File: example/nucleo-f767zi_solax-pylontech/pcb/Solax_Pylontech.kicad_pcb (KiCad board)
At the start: 2 copper layers, 34 x 86 mm, 37 parts, among them J1 Conn_02x10_Odd_Even, J2 Conn_02x07_Odd_Even, U1 LT1107CS, U2 MCP2551-I-SN, U3 MCP2551-I-SN

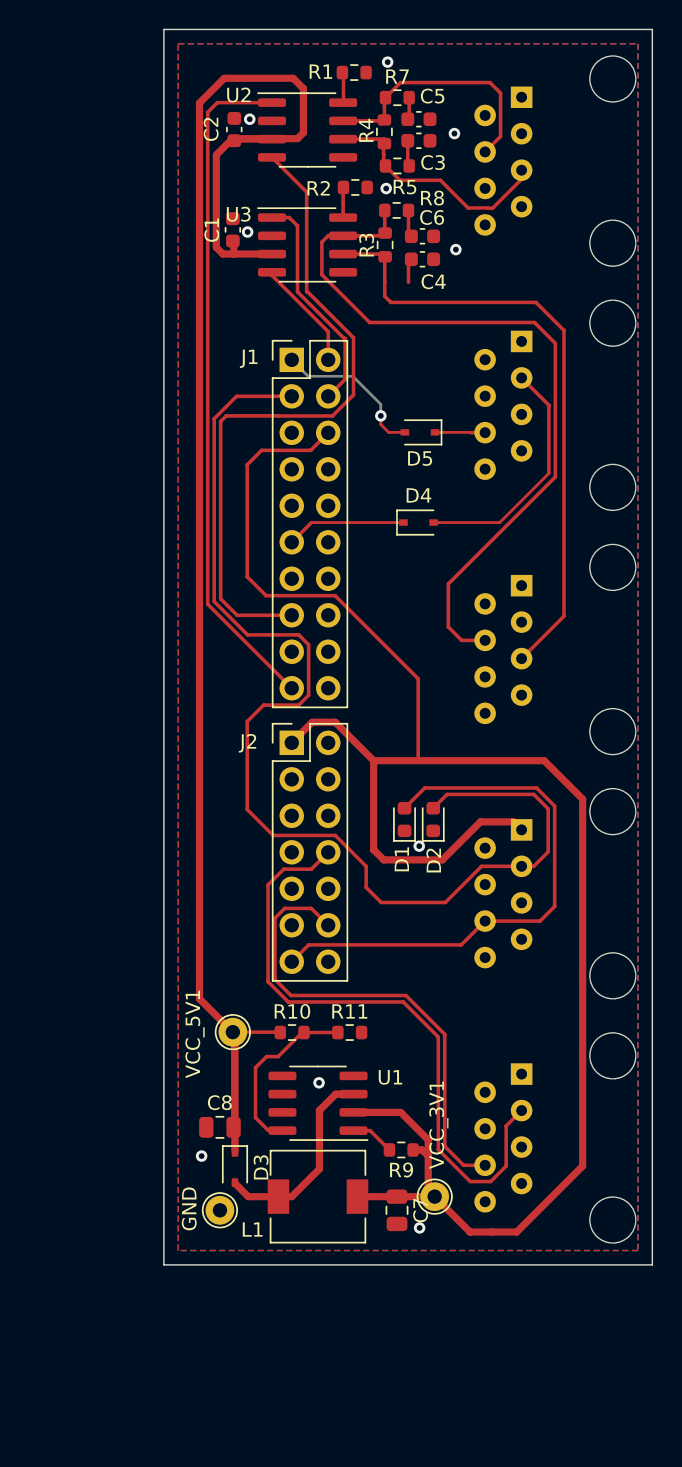
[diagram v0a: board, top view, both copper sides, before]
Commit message: - implement battery balancing using external charger in front of each pack (HDR-15-48), each one driven by a triac module (MRA-23D2) - add home assistant shenanigans to drive the battery balancing (manual or automatic)
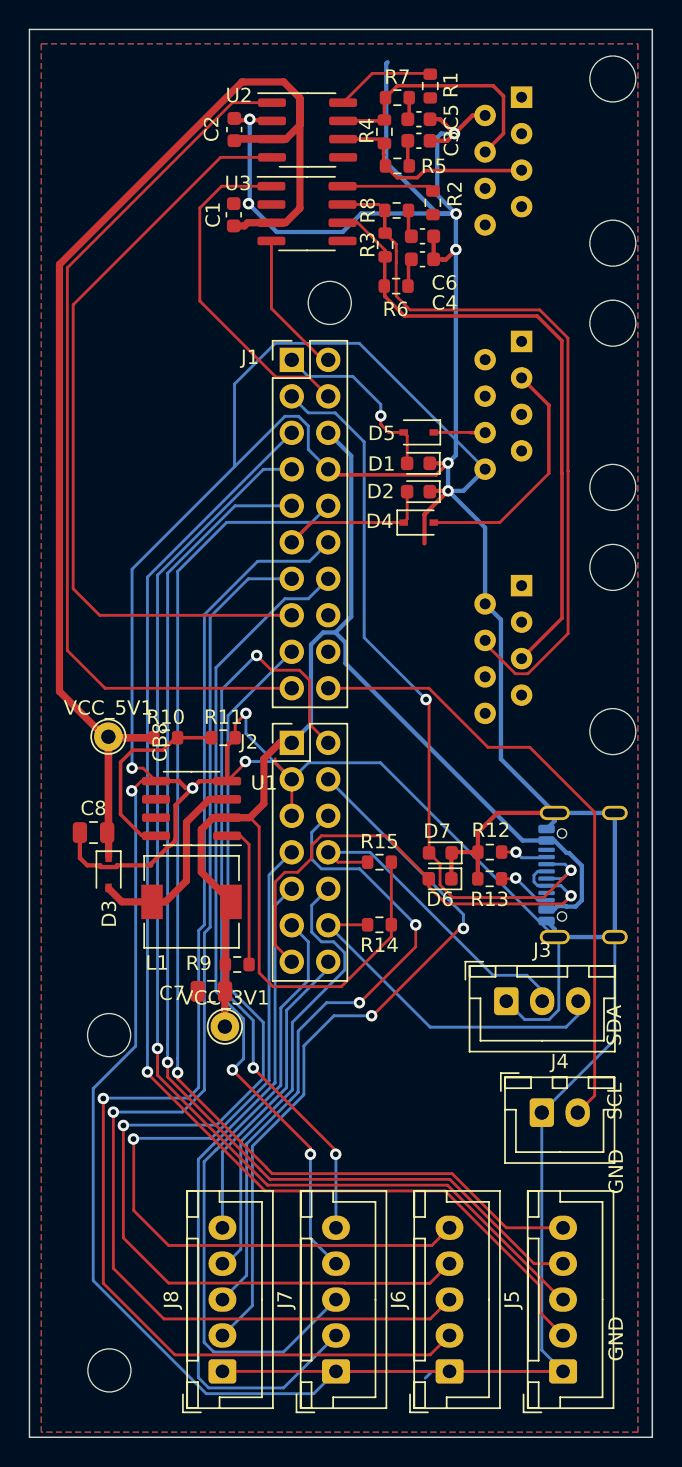
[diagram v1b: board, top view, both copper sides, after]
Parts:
- removed GND: TestPoint_THTPad_D2.0mm_Drill1.0mm, TestPoint:TestPoint_THTPad_D2.0mm_Drill1.0mm
- removed JI2CMON1: RJ45, Connector_RJ:RJ45_Amphenol_54602-x08_Horizontal
- added D6: D_TVS, Diode_SMD:D_0603_1608Metric, F.Cu at (83.2, 140.1)
- added D7: D_TVS, Diode_SMD:D_0603_1608Metric, F.Cu at (83.2, 138.3)
- added H1: MountingHole, MountingHole:MountingHole_3mm, F.Cu at (60.2, 151.0)
- added H2: MountingHole, MountingHole:MountingHole_3mm, F.Cu at (60.2, 174.3)
- added H3: MountingHole, MountingHole:MountingHole_3mm, F.Cu at (75.5, 100.0)
- added J3: Conn_01x03_Socket, Connector_JST:JST_XH_B3B-XH-A_1x03_P2.50mm_Vertical, F.Cu at (87.8, 148.6)
- added J4: Conn_01x02_Socket, Connector_JST:JST_XH_B2B-XH-A_1x02_P2.50mm_Vertical, F.Cu at (90.3, 156.4)
- added J5: Conn_01x05_Socket, Connector_JST:JST_XH_B5B-XH-A_1x05_P2.50mm_Vertical, F.Cu at (91.8, 174.4)
- added J6: Conn_01x05_Socket, Connector_JST:JST_XH_B5B-XH-A_1x05_P2.50mm_Vertical, F.Cu at (83.9, 174.4)
- added J7: Conn_01x05_Socket, Connector_JST:JST_XH_B5B-XH-A_1x05_P2.50mm_Vertical, F.Cu at (76.0, 174.4)
- added J8: Conn_01x05_Socket, Connector_JST:JST_XH_B5B-XH-A_1x05_P2.50mm_Vertical, F.Cu at (68.1, 174.4)
- added R12: 5k1, Resistor_SMD:R_0603_1608Metric, F.Cu at (86.7, 138.3)
- added R13: 5k1, Resistor_SMD:R_0603_1608Metric, F.Cu at (86.7, 140.1)
- added R14: 4k7, Resistor_SMD:R_0603_1608Metric, F.Cu at (79.0, 143.3)
- added R15: 4k7, Resistor_SMD:R_0603_1608Metric, F.Cu at (79.0, 139.0)
- added R6: 100, Resistor_SMD:R_0603_1608Metric, F.Cu at (80.2, 98.9)
- JUARTINV1: value RJ45 -> USB_C_Receptacle_USB2.0_16P; footprint Connector_RJ:RJ45_Amphenol_54602-x08_Horizontal -> Connector_USB:USB_C_Receptacle_GCT_USB4105-xx-A_16P_TopMnt_Horizontal
- moved D1 24.8 mm to (81.7, 111.2), turned to 180 degrees
- moved D2 22.8 mm to (81.7, 113.2), turned to 180 degrees
- moved C8 22.3 mm to (59.1, 136.9)
- moved L1 22.3 mm to (65.9, 141.7)
- moved U1 22.3 mm to (65.9, 135.2)
- moved D3 22.3 mm to (60.1, 139.7)
- moved R10 22.3 mm to (64.1, 130.3)
- moved R11 22.3 mm to (68.1, 130.3)
- moved VCC_5V1 22.3 mm to (60.1, 130.2)
- moved C7 20.0 mm to (67.3, 148.0), turned to 180 degrees
- moved VCC_3V1 18.8 mm to (68.2, 150.4)
- moved R9 17.2 mm to (69.1, 146.1), turned to 0 degrees
- moved JUARTINV1 6.26 mm to (94.3, 139.9)
- moved R2 5.50 mm to (82.7, 93.1), turned to -90 degrees
- moved R1 5.37 mm to (82.5, 84.9), turned to -90 degrees
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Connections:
- D1 pad 2: UART1_TX_INV -> UART6_TX_BMS
- D2 pad 2: UART1_RX_INV -> UART6_RX_BMS
- J1 pad 10: unconnected-(J1-Pad10) -> SW_CHBAT4
- J1 pad 12: unconnected-(J1-Pad12) -> SW_CHBAT5
- J1 pad 13: unconnected-(J1-Pad13) -> SW_CHBAT6
- J1 pad 14: unconnected-(J1-Pad14) -> SW_CHBAT11
- J1 pad 17: unconnected-(J1-Pad17) -> SW_CHBAT7
- J1 pad 5: unconnected-(J1-Pad5) -> SW_CHBAT1
- J1 pad 7: unconnected-(J1-Pad7) -> SW_CHBAT2
- J1 pad 9: unconnected-(J1-Pad9) -> SW_CHBAT3
- J2 pad 10: unconnected-(J2-Pad10) -> SW_CHBAT15
- J2 pad 11: unconnected-(J2-Pad11) -> SW_CHBAT10
- J2 pad 14: unconnected-(J2-Pad14) -> SW_CHBAT16
- J2 pad 2: unconnected-(J2-Pad2) -> SW_CHBAT12
- J2 pad 4: unconnected-(J2-Pad4) -> SW_CHBAT13
- J2 pad 6: unconnected-(J2-Pad6) -> SW_CHBAT14
- J2 pad 7: unconnected-(J2-Pad7) -> SW_CHBAT8
- J2 pad 9: unconnected-(J2-Pad9) -> SW_CHBAT9
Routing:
- net GND: track 0.89 -> 423.3 mm, vias 10 -> 12
- net SW_CHBAT5: track 0.00 -> 90.4 mm, vias 0 -> 1
- net SW_CHBAT1: track 0.00 -> 86.3 mm, vias 0 -> 1
- net SW_CHBAT6: track 0.00 -> 83.2 mm, vias 0 -> 1
- net SW_CHBAT2: track 0.00 -> 81.9 mm, vias 0 -> 1
- net SW_CHBAT4: track 0.00 -> 78.8 mm, vias 0 -> 1
- net SW_CHBAT3: track 0.00 -> 78.6 mm, vias 0 -> 1
- net VCC_5V: track 182.8 -> 106.0 mm
- net SW_CHBAT7: track 0.00 -> 76.0 mm, vias 0 -> 1
- net SW_CHBAT8: track 0.00 -> 56.8 mm, vias 0 -> 1
- net SW_CHBAT11: track 0.00 -> 56.0 mm, vias 0 -> 2
- net SW_CHBAT12: track 0.00 -> 53.5 mm, vias 0 -> 3
- net SW_CHBAT13: track 0.00 -> 51.3 mm, vias 0 -> 2
- net SW_CHBAT9: track 0.00 -> 48.1 mm
- net SW_CHBAT14: track 0.00 -> 45.6 mm, vias 0 -> 2
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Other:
- board size 34 x 86 mm -> 43.4 x 98 mm
- board text added: "CB8"
- board text added: "GND"
- board text added: "SCL"
- board text added: "SDA"
